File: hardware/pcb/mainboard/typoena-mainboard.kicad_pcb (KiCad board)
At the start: 2 copper layers, 50 x 70 mm, 34 parts, among them J1 DESPI-C579, J2 UART-PROG, J3 MT3608-IN, J4 MT3608-OUT-5V, J5 BTN-JST-XH, J6 HARNESS-PCB2, Q1 AO3401A, Q2 AO3401A, Q3 2N7002, SW1 RESET, SW2 BOOT, U1 ESP32-S3-WROOM-1-N16R8, U2 AMS1117-3.3

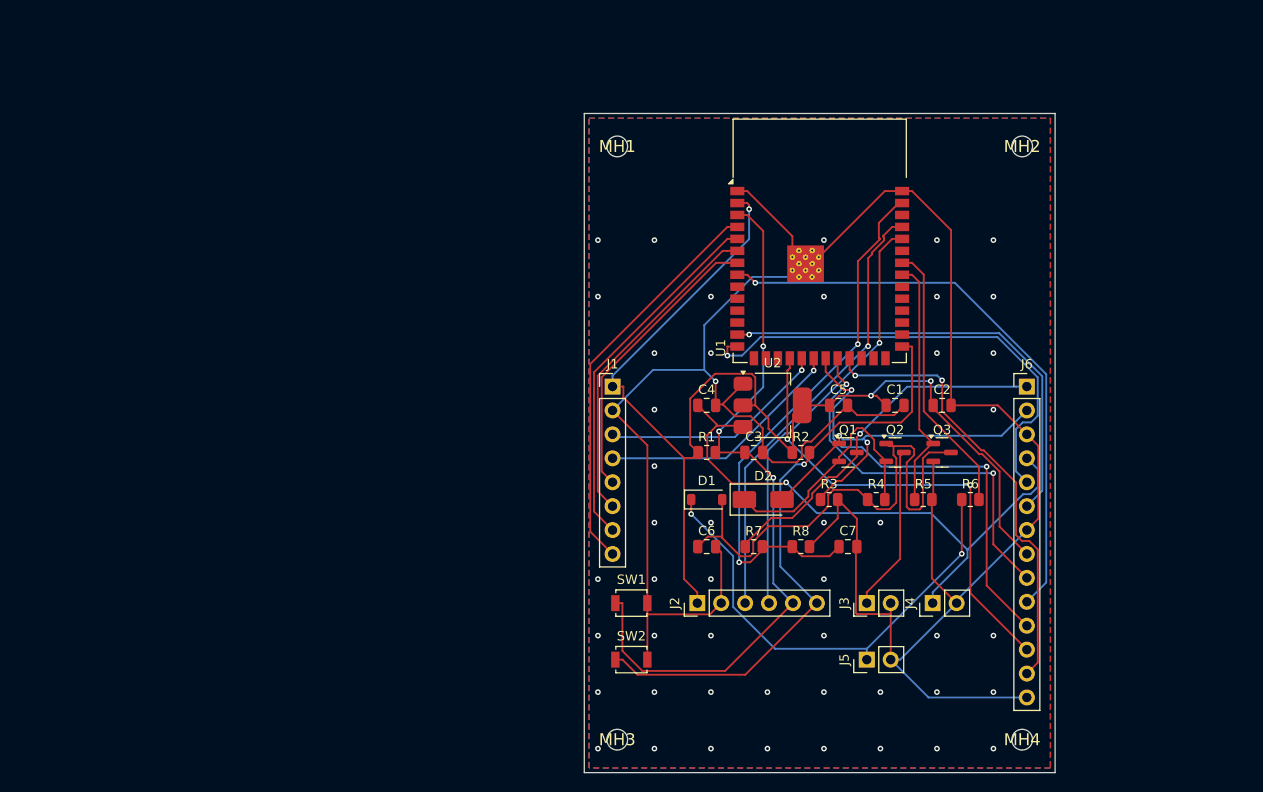
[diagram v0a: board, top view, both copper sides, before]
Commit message: refactor(pcb): collapse to a single mainboard project
The two-perfboard design around the DevKitC-1 is gone; mainboard-v2 takes
the mainboard/ name and the -v2 suffix leaves every filename. The KiCad
project name is rewritten inside the instance blocks of all five sheets
too, otherwise KiCad drops the footprint assignments on open. ERC and DRC
still report 0 violations.

Add a Ground net class, split off Power, so GND carries its own via size
for the stitching and shows up in its own colour while routing. Its 0.2 mm
clearance is the neutral value: clearance resolves to the larger of the two
classes, so it never widens a gap on its own.

Drop the GPIO table from hardware/pcb/README.md rather than move it — the
netlist disagrees with it. PWR_HOLD no longer exists, PWR_SENSE is IO21 and
not IO41, and battery level comes from the BQ25896 over I2C instead of an
ADC. mainboard/README.md carries the pin plan that ships. wiring.md keeps
its bench-build pinout but stops attributing it to the deleted board.

hardware/bom.md, hardware/wiring.md and hardware/case/ still describe the
bench build, tracked as a TODO in the mainboard README.

Co-Authored-By: Claude Opus 5 <noreply@anthropic.com>
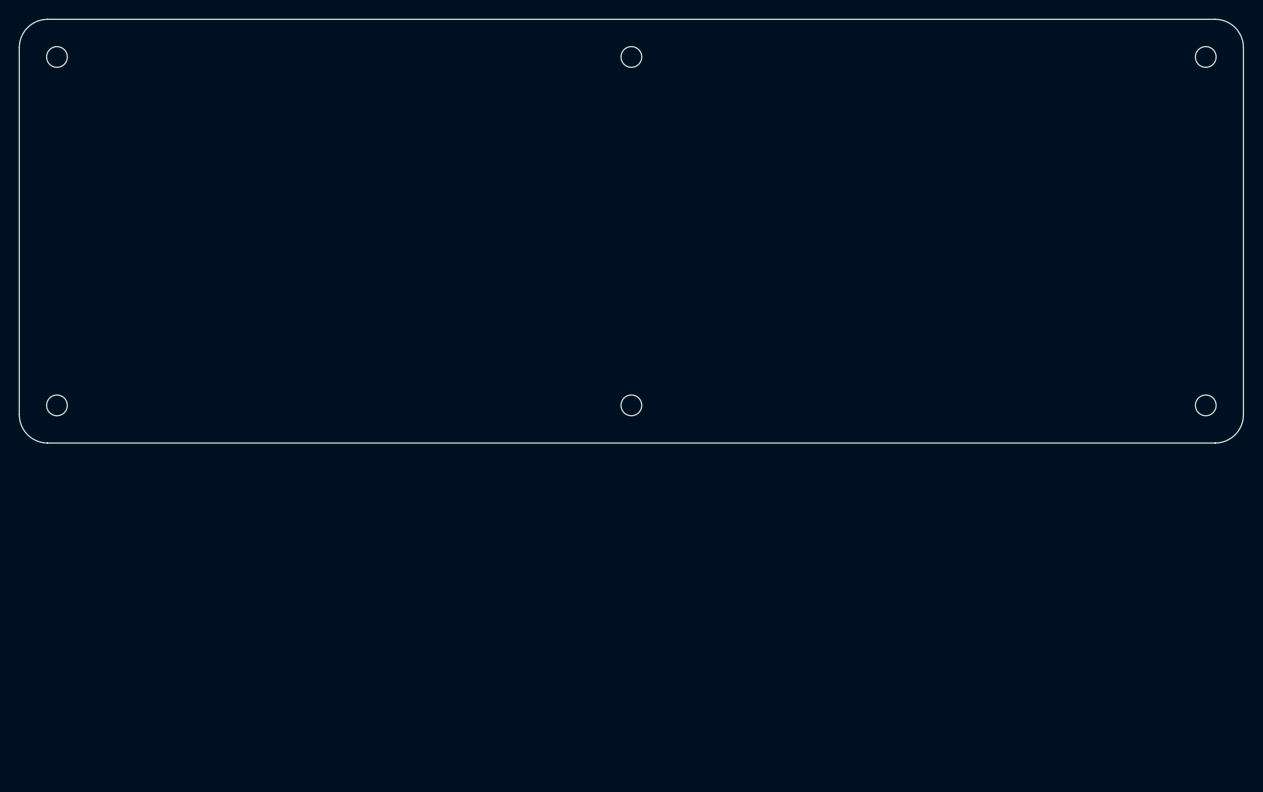
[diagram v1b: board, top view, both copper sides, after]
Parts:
- removed C1, C6, C7: 100nF, Capacitor_SMD:C_0805_2012Metric
- removed C2: 10uF, Capacitor_SMD:C_0805_2012Metric
- removed C3: 1uF, Capacitor_SMD:C_0805_2012Metric
- removed C4, C5: 22uF, Capacitor_SMD:C_0805_2012Metric
- removed D1: 1N4148W, Diode_SMD:D_SOD-123
- removed D2: SS34, Diode_SMD:D_SMA
- removed J1: DESPI-C579, Connector_PinHeader_2.54mm:PinHeader_1x08_P2.54mm_Vertical
- removed J2: UART-PROG, Connector_PinHeader_2.54mm:PinHeader_1x06_P2.54mm_Vertical
- removed J3: MT3608-IN, Connector_PinHeader_2.54mm:PinHeader_1x02_P2.54mm_Vertical
- removed J4: MT3608-OUT-5V, Connector_PinHeader_2.54mm:PinHeader_1x02_P2.54mm_Vertical
- removed J5: BTN-JST-XH, Connector_PinHeader_2.54mm:PinHeader_1x02_P2.54mm_Vertical
- removed J6: HARNESS-PCB2, Connector_PinHeader_2.54mm:PinHeader_1x14_P2.54mm_Vertical
- removed Q1, Q2: AO3401A, Package_TO_SOT_SMD:SOT-23
- removed Q3: 2N7002, Package_TO_SOT_SMD:SOT-23
- removed R1, R2, R6: 10k, Resistor_SMD:R_0805_2012Metric
- removed R3, R4, R5, R7, R8: 100k, Resistor_SMD:R_0805_2012Metric
- removed SW1: RESET, Button_Switch_SMD:SW_SPST_B3U-1000P
- removed SW2: BOOT, Button_Switch_SMD:SW_SPST_B3U-1000P
- removed U1: ESP32-S3-WROOM-1-N16R8, RF_Module:ESP32-S3-WROOM-1
- removed U2: AMS1117-3.3, Package_TO_SOT_SMD:SOT-223-3_TabPin2
- added MH5: MountingHole_2.2mm_M2, MountingHole:MountingHole_2.2mm_M2, F.Cu at (105.0, 81.0)
- added MH6: MountingHole_2.2mm_M2, MountingHole:MountingHole_2.2mm_M2, F.Cu at (166.0, 81.0)
- MH1, MH2, MH3, MH4: value MountingHole_2.2mm -> MountingHole_2.2mm_M2; footprint MountingHole:MountingHole_2.2mm -> MountingHole:MountingHole_2.2mm_M2
- moved MH4 108.5 mm to (44.0, 81.0)
- moved MH3 95.7 mm to (166.0, 44.0)
- moved MH1 60.3 mm to (44.0, 44.0)
- moved MH2 42.6 mm to (105.0, 44.0)
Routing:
- net GND: track 267.2 -> 0.00 mm, vias 48 -> 0
- net +3V3: track 125.9 -> 0.00 mm, vias 3 -> 0
- net EN: track 78.2 -> 0.00 mm, vias 3 -> 0
- net IO0: track 65.3 -> 0.00 mm, vias 1 -> 0
- net V5: track 62.5 -> 0.00 mm, vias 1 -> 0
- net SD_MOSI: track 62.2 -> 0.00 mm, vias 1 -> 0
- net LATCH_GATE: track 58.0 -> 0.00 mm
- net VBAT_SENSE: track 58.0 -> 0.00 mm, vias 2 -> 0
- net USB_DP: track 50.6 -> 0.00 mm, vias 1 -> 0
- net BTN: track 50.5 -> 0.00 mm, vias 2 -> 0
- net SD_CS: track 50.1 -> 0.00 mm, vias 2 -> 0
- net USB_DM: track 48.8 -> 0.00 mm, vias 1 -> 0
- net CHRG: track 48.0 -> 0.00 mm, vias 2 -> 0
- net UART_TX: track 47.7 -> 0.00 mm, vias 1 -> 0
- net SD_MISO: track 47.1 -> 0.00 mm, vias 2 -> 0
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- removed copper zone on B.Cu, net GND
- removed copper zone on F.Cu, net GND
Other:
- board size 50 x 70 mm -> 130 x 45 mm
- copper layers 2 -> 4

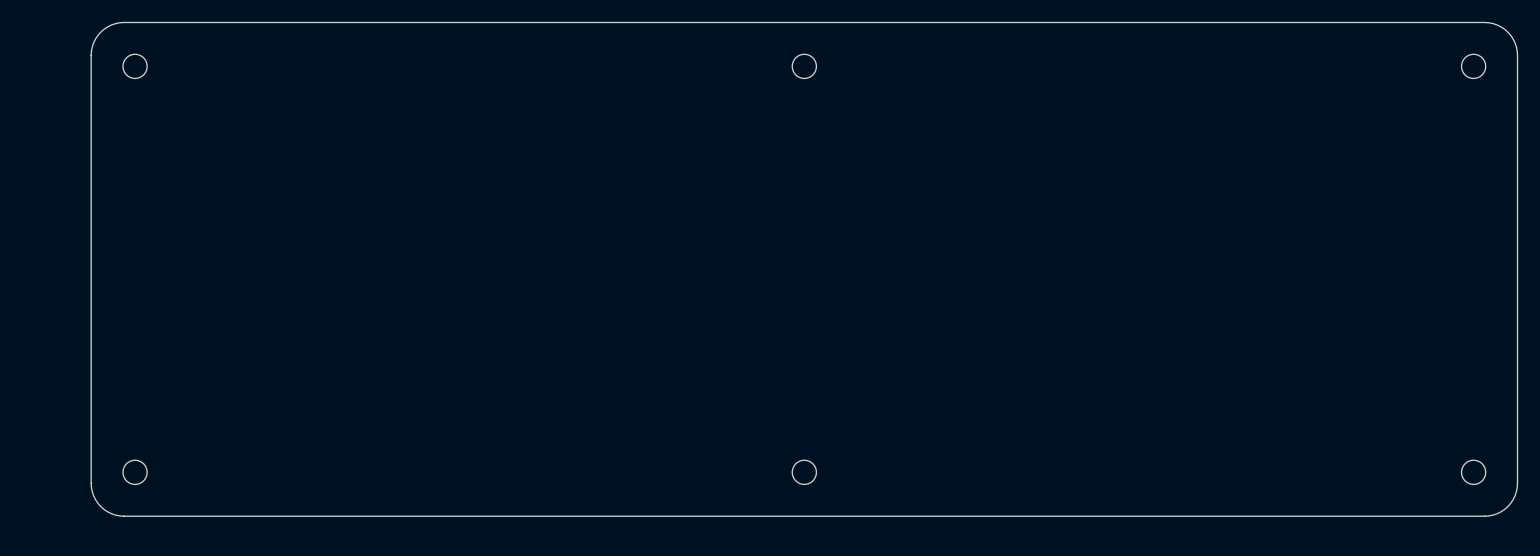
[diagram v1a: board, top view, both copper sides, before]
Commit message: feat(pcb): import and place all 98 footprints
Connectors, ICs, inductors and passives placed inside the outline. J6, J7
and J8 pulled inward (0.35/0.35/0.20mm) so their copper clears the milled
edge by 0.5mm — the USB-C shield posts sat at 0.15mm, under JLCPCB's floor.

DRC clean apart from the 264 unrouted ratsnest items.

Co-Authored-By: Claude Opus 5 <noreply@anthropic.com>
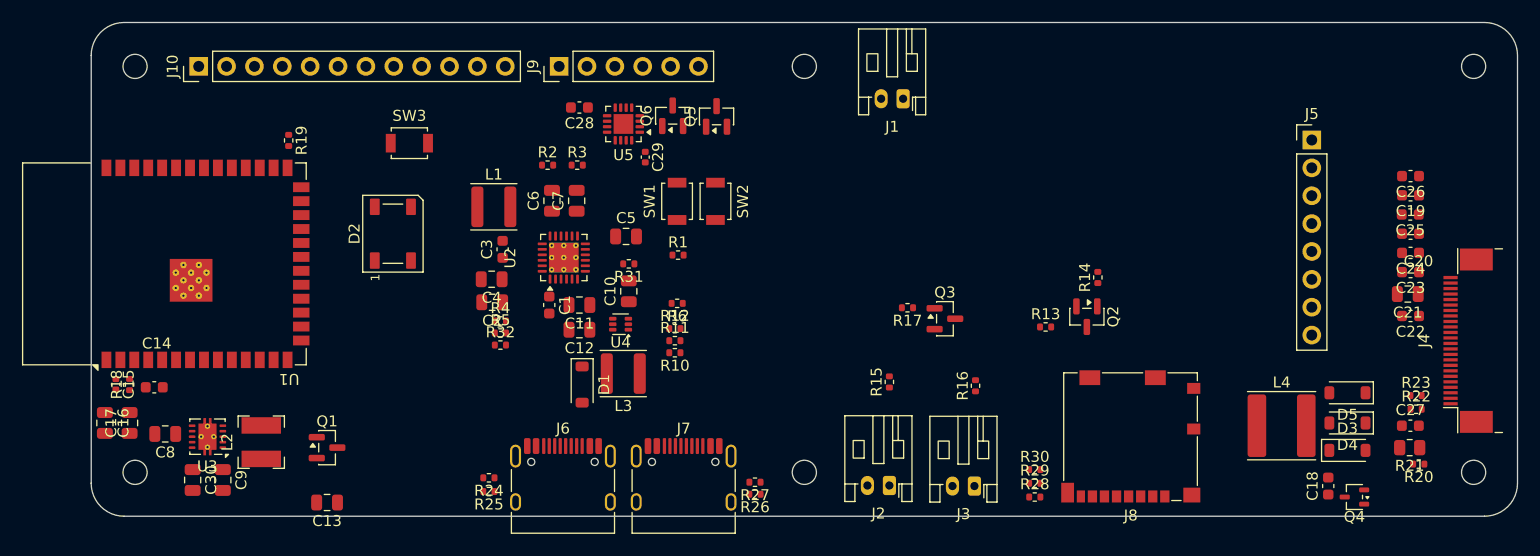
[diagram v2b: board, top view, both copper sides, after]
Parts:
- added C1: 1uF, Capacitor_SMD:C_0603_1608Metric, F.Cu at (81.8, 65.8)
- added C10: 10uF, Capacitor_SMD:C_0805_2012Metric, F.Cu at (89.0, 64.5)
- added C11: 22uF, Capacitor_SMD:C_0805_2012Metric, F.Cu at (84.5, 65.8)
- added C12: 22uF, Capacitor_SMD:C_0805_2012Metric, F.Cu at (84.5, 68.0)
- added C13: 10uF, Capacitor_SMD:C_0805_2012Metric, F.Cu at (61.5, 83.8)
- added C14: 1uF, Capacitor_SMD:C_0603_1608Metric, F.Cu at (45.8, 73.2)
- added C15: 100nF, Capacitor_SMD:C_0402_1005Metric, F.Cu at (42.2, 73.0)
- added C16: 10uF, Capacitor_SMD:C_0805_2012Metric, F.Cu at (41.2, 76.5)
- added C17: 22uF, Capacitor_SMD:C_0805_2012Metric, F.Cu at (43.5, 76.5)
- added C18: 1uF, Capacitor_SMD:C_0603_1608Metric, F.Cu at (152.8, 82.2)
- added C19: 1uF, Capacitor_SMD:C_0603_1608Metric, F.Cu at (160.2, 55.8)
- added C2: 10uF, Capacitor_SMD:C_0805_2012Metric, F.Cu at (76.5, 65.5)
- added C20: 1uF, Capacitor_SMD:C_0603_1608Metric, F.Cu at (160.2, 59.2)
- added C21: 4.7uF, Capacitor_SMD:C_0805_2012Metric, F.Cu at (160.0, 64.8)
- added C22: 1uF, Capacitor_SMD:C_0603_1608Metric, F.Cu at (160.2, 66.8)
- added C23: 1uF, Capacitor_SMD:C_0603_1608Metric, F.Cu at (160.2, 62.8)
- added C24: 1uF, Capacitor_SMD:C_0603_1608Metric, F.Cu at (160.2, 61.0)
- added C25: 1uF, Capacitor_SMD:C_0603_1608Metric, F.Cu at (160.2, 57.5)
- added C26: 1uF, Capacitor_SMD:C_0603_1608Metric, F.Cu at (160.2, 54.0)
- added C27: 1uF, Capacitor_SMD:C_0603_1608Metric, F.Cu at (160.2, 76.8)
- added C28: 1uF, Capacitor_SMD:C_0603_1608Metric, F.Cu at (84.5, 47.8)
- added C29: 100nF, Capacitor_SMD:C_0402_1005Metric, F.Cu at (90.5, 52.3)
- added C3: 47nF, Capacitor_SMD:C_0603_1608Metric, F.Cu at (77.5, 60.7)
- added C30: 10uF, Capacitor_SMD:C_0805_2012Metric, F.Cu at (49.2, 81.7)
- added C4: 4.7uF, Capacitor_SMD:C_0805_2012Metric, F.Cu at (76.5, 63.4)
- added C5: 10uF, Capacitor_SMD:C_0805_2012Metric, F.Cu at (88.8, 59.5)
- added C6: 10uF, Capacitor_SMD:C_0805_2012Metric, F.Cu at (82.0, 56.2)
- added C7: 10uF, Capacitor_SMD:C_0805_2012Metric, F.Cu at (84.2, 56.2)
- added C8: 10uF, Capacitor_SMD:C_0805_2012Metric, F.Cu at (46.8, 77.5)
- added C9: 10uF, Capacitor_SMD:C_0805_2012Metric, F.Cu at (52.0, 81.7)
- added D1: SMF5.0A, Diode_SMD:D_SOD-123, F.Cu at (84.8, 73.0)
- added D2: WS2812B, LED_SMD:LED_WS2812B_PLCC4_5.0x5.0mm_P3.2mm, F.Cu at (67.5, 59.2)
- added D3: B5819W, Diode_SMD:D_SOD-123, F.Cu at (154.5, 79.0)
- added D4: B5819W, Diode_SMD:D_SOD-123, F.Cu at (154.5, 76.5)
- added D5: B5819W, Diode_SMD:D_SOD-123, F.Cu at (154.5, 73.8)
- added J1: BATTERIE JST-PH, Connector_JST:JST_PH_S2B-PH-K_1x02_P2.00mm_Horizontal, F.Cu at (114.0, 47.0)
- added J10: EXTENSION (non monte), Connector_PinHeader_2.54mm:PinHeader_1x12_P2.54mm_Vertical, F.Cu at (49.8, 44.0)
- added J2: BOUTON contact JST-PH, Connector_JST:JST_PH_S2B-PH-K_1x02_P2.00mm_Horizontal, F.Cu at (112.8, 82.2)
- added J3: BOUTON LED JST-PH, Connector_JST:JST_PH_S2B-PH-K_1x02_P2.00mm_Horizontal, F.Cu at (120.5, 82.2)
- added J4: FPC 24p 0.5mm - PANNEAU, Connector_FFC-FPC:Jushuo_AFC07-S24FCA-00_1x24-1MP_P0.50_Horizontal, F.Cu at (165.5, 69.0)
- added J5: SECOURS DESPI-C579, Connector_PinHeader_2.54mm:PinHeader_1x08_P2.54mm_Vertical, F.Cu at (151.2, 50.7)
- added J6: USB-C CHARGE + PROG, Connector_USB:USB_C_Receptacle_HRO_TYPE-C-31-M-12, F.Cu at (83.0, 82.7)
- added J7: USB-C CLAVIER (hote), Connector_USB:USB_C_Receptacle_HRO_TYPE-C-31-M-12, F.Cu at (94.0, 82.7)
- added J8: microSD, Connector_Card:microSD_HC_Molex_104031-0811, F.Cu at (134.8, 77.8)
- added J9: UART PROG, Connector_PinHeader_2.54mm:PinHeader_1x06_P2.54mm_Vertical, F.Cu at (82.7, 44.0)
- added L1: 1uH 4.15A, Inductor_SMD:L_APV_ANR4030, F.Cu at (76.7, 56.8)
- added L2: 2.2uH 2.9A, Inductor_SMD:L_Bourns-SRN4018, F.Cu at (55.5, 78.2)
- added L3: 1uH 4.15A, Inductor_SMD:L_APV_ANR4030, F.Cu at (88.5, 72.0)
- added L4: 47uH 1.2A, Inductor_SMD:L_APV_ANR6045, F.Cu at (148.5, 76.8)
- added Q1: AO3401A, Package_TO_SOT_SMD:SOT-23, F.Cu at (61.5, 78.8)
- added Q2: 2N7002, Package_TO_SOT_SMD:SOT-23, F.Cu at (130.8, 66.8)
- added Q3: 2N7002, Package_TO_SOT_SMD:SOT-23, F.Cu at (117.8, 67.0)
- added Q4: Si1308EDL, Package_TO_SOT_SMD:SOT-323_SC-70, F.Cu at (155.1, 83.2)
- added Q5: 2N7002, Package_TO_SOT_SMD:SOT-23, F.Cu at (97.0, 48.6)
- added Q6: 2N7002, Package_TO_SOT_SMD:SOT-23, F.Cu at (93.0, 48.5)
- added R1: 150R, Resistor_SMD:R_0402_1005Metric, F.Cu at (93.5, 61.2)
- added R10: 510k, Resistor_SMD:R_0402_1005Metric, F.Cu at (93.2, 70.1)
- added R11: 68k, Resistor_SMD:R_0402_1005Metric, F.Cu at (93.2, 69.0)
- added R12: 100k, Resistor_SMD:R_0402_1005Metric, F.Cu at (93.2, 67.9)
- added R13: 100k, Resistor_SMD:R_0402_1005Metric, F.Cu at (127.0, 67.8)
- added R14: 100k, Resistor_SMD:R_0402_1005Metric, F.Cu at (131.8, 63.2)
- added R15: 10k, Resistor_SMD:R_0402_1005Metric, F.Cu at (112.8, 72.8)
- added R16: 100R, Resistor_SMD:R_0402_1005Metric, F.Cu at (120.6, 73.1)
- added R17: 100k, Resistor_SMD:R_0402_1005Metric, F.Cu at (114.4, 66.0)
- added R18: 10k, Resistor_SMD:R_0402_1005Metric, F.Cu at (43.5, 73.0)
- added R19: 10k, Resistor_SMD:R_0402_1005Metric, F.Cu at (58.0, 50.8)
- added R2: 10k, Resistor_SMD:R_0402_1005Metric, F.Cu at (81.6, 53.0)
- added R20: 1M, Resistor_SMD:R_0402_1005Metric, F.Cu at (161.0, 80.2)
- added R21: 2R2, Resistor_SMD:R_0805_2012Metric, F.Cu at (160.2, 78.8)
- added R22: 10k, Resistor_SMD:R_0402_1005Metric, F.Cu at (160.8, 75.2)
- added R23: 10k, Resistor_SMD:R_0402_1005Metric, F.Cu at (160.8, 74.0)
- added R24: 5k1 1%, Resistor_SMD:R_0402_1005Metric, F.Cu at (76.2, 81.5)
- added R25: 5k1 1%, Resistor_SMD:R_0402_1005Metric, F.Cu at (76.2, 82.8)
- added R26: 56k 1%, Resistor_SMD:R_0402_1005Metric, F.Cu at (100.5, 83.0)
- added R27: 56k 1%, Resistor_SMD:R_0402_1005Metric, F.Cu at (100.5, 81.9)
- added R28: 10k, Resistor_SMD:R_0402_1005Metric, F.Cu at (126.0, 83.2)
- added R29: 10k, Resistor_SMD:R_0402_1005Metric, F.Cu at (126.0, 82.0)
- added R3: 12k, Resistor_SMD:R_0402_1005Metric, F.Cu at (84.3, 53.0)
- added R30: 10k, Resistor_SMD:R_0402_1005Metric, F.Cu at (126.0, 80.8)
- added R31: 4k7, Resistor_SMD:R_0402_1005Metric, F.Cu at (89.0, 62.0)
- added R32: 4k7, Resistor_SMD:R_0402_1005Metric, F.Cu at (77.3, 69.4)
- added R4: 10k, Resistor_SMD:R_0402_1005Metric, F.Cu at (77.3, 67.2)
- added R5: 10k, Resistor_SMD:R_0402_1005Metric, F.Cu at (77.3, 68.3)
- added R6: 10k, Resistor_SMD:R_0402_1005Metric, F.Cu at (93.4, 65.6)
- added SW1: QON, Button_Switch_SMD:SW_SPST_B3U-1000P, F.Cu at (93.4, 56.3)
- added SW2: RESET, Button_Switch_SMD:SW_SPST_B3U-1000P, F.Cu at (96.9, 56.3)
- added SW3: BOOT, Button_Switch_SMD:SW_SPST_B3U-1000P, F.Cu at (69.0, 51.0)
- added U1: ESP32-S3-WROOM-1-N16R8, RF_Module:ESP32-S3-WROOM-1, F.Cu at (46.6, 62.0)
- added U2: BQ25896RTW, Package_DFN_QFN:Texas_RTW_WQFN-24-1EP_4x4mm_P0.5mm_EP2.7x2.7mm_ThermalVias, F.Cu at (83.1, 61.4)
- added U3: TPS63001DRCR, Package_SON:Texas_DRC0010J_ThermalVias, F.Cu at (50.6, 77.8)
- added U4: TPS61023DRL, Package_TO_SOT_SMD:SOT-563, F.Cu at (88.2, 67.5)
- added U5: CH343P, Package_DFN_QFN:WCH_QFN-16-1EP_3x3mm_P0.5mm_EP1.8x1.8mm, F.Cu at (88.5, 49.2)
